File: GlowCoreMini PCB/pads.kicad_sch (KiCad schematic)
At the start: 15 parts, among them P10 Solder_Pad, P11 Solder_Pad, P13 Solder_Pad, P14 Solder_Pad, P19 Solder_Pad, P20 Solder_Pad, P21 Solder_Pad, P22 Solder_Pad, P4 Solder_Pad, P5 Solder_Pad, P6 Solder_Pad, P7 Solder_Pad, P8 Solder_Pad, P9 Solder_Pad

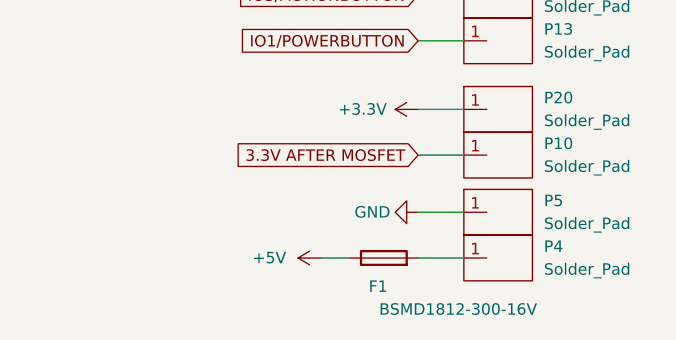
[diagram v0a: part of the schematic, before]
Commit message: split up schematic
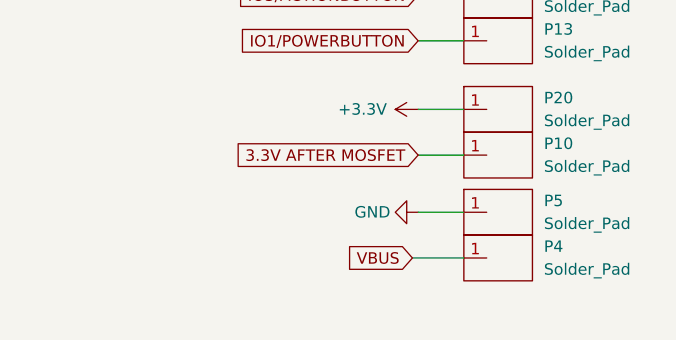
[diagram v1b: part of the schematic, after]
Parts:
- removed F1: BSMD1812-300-16V, Fuse:Fuse_1812_4532Metric_Pad1.30x3.40mm_HandSolder, symbol Device:Fuse
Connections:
- net VBUS: now reaches P4.1
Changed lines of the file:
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@@
-    (stroke (width 0) (type default))
-  )
-  (wire (pts (xy 83.185 125.73) (xy 86.36 125.73))
     (stroke (width 0) (type default))
   )
@@
     (stroke (width 0) (type default))
   )
-  (wire (pts (xy 93.98 125.73) (xy 99.06 125.73))
+  (wire (pts (xy 93.345 125.73) (xy 99.06 125.73))
     (stroke (width 0) (type default))
   )
@@
     (effects (font (size 1.27 1.27)) (justify right))
     (property "Intersheetrefs" "${INTERSHEET_REFS}" (at 78.0807 62.1506 0)
+      (effects (font (size 1.27 1.27)) (justify right) hide)
+    )
+  )
+  (global_label "VBUS" (shape input) (at 93.345 125.73 180) (fields_autoplaced)
+    (effects (font (size 1.27 1.27)) (justify right))
+    (property "Intersheetrefs" "${INTERSHEET_REFS}" (at 85.6949 125.73 0)
       (effects (font (size 1.27 1.27)) (justify right) hide)
     )
@@
     )
   )
-  (symbol (lib_id "power:+5V") (at 83.185 125.73 90) (unit 1)
-    (in_bom yes) (on_board yes) (dnp no)
-    (property "Reference" "#PWR0147" (at 86.995 125.73 0)
-      (effects (font (size 1.27 1.27)) hide)
-    )
-    (property "Value" "+5V" (at 75.565 125.73 90)
-      (effects (font (size 1.27 1.27)) (justify right))
-    )
-    (property "Footprint" "" (at 83.185 125.73 0)
-      (effects (font (size 1.27 1.27)) hide)
-    )
-    (property "Datasheet" "" (at 83.185 125.73 0)
-      (effects (font (size 1.27 1.27)) hide)
-    )
-    (pin "1")
-    (instances
-      (project "GlowCoreMini PCB"
-        (path "/c6f71574-e06f-4ae6-b347-b6a4861b944a"
-          (reference "#PWR0147") (unit 1)
-        )
-        (path "/c6f71574-e06f-4ae6-b347-b6a4861b944a/0f01344c-3202-44f7-86d1-34a5ac107bfa"
-          (reference "#PWR0147") (unit 1)
-        )
-      )
-    )
-  )
   (symbol (lib_id "MyParts:Solder_Pad") (at 99.06 90.17 0) (unit 1)
     (in_bom yes) (on_board yes) (dnp no) (fields_autoplaced)
@@
         )
       )
-    )
-  )
-  (symbol (lib_id "Device:Fuse") (at 90.17 125.73 90) (unit 1)
-    (in_bom yes) (on_board yes) (dnp no)
-    (property "Reference" "F1" (at 89.535 128.905 90)
-      (effects (font (size 1.27 1.27)))
-    )
-    (property "Value" "BSMD1812-300-16V" (at 98.425 131.445 90)
-      (effects (font (size 1.27 1.27)))
-    )
-    (property "Footprint" "Fuse:Fuse_1812_4532Metric_Pad1.30x3.40mm_HandSolder" (at 90.17 127.508 90)
-      (effects (font (size 1.27 1.27)) hide)
-    )
-    (property "Datasheet" "" (at 90.17 125.73 0)
-      (effects (font (size 1.27 1.27)) hide)
-    )
-    (property "LCSC #" "C883162" (at 90.17 125.73 90)
-      (effects (font (size 1.27 1.27)) hide)
-    )
-    (pin "1")
-    (pin "2")
-    (instances
-      (project "GlowCoreMini PCB"
-        (path "/c6f71574-e06f-4ae6-b347-b6a4861b944a"
-          (reference "F1") (unit 1)
-        )
-        (path "/c6f71574-e06f-4ae6-b347-b6a4861b944a/0f01344c-3202-44f7-86d1-34a5ac107bfa"
-          (reference "F1") (unit 1)
-        )
-      )
